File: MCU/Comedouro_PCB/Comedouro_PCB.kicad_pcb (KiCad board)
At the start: 2 copper layers, 19 parts, among them J1 Conn_02x10_Odd_Even, J2 Conn_02x10_Odd_Even, J5 HC-SR04, M1 Motor_Servo, Q1 Q_NPN_CBE, SW1 SW_Push, SW2 SW_Push, SW3 SW_Push, SW4 SW_Push, SW5 SW_Push

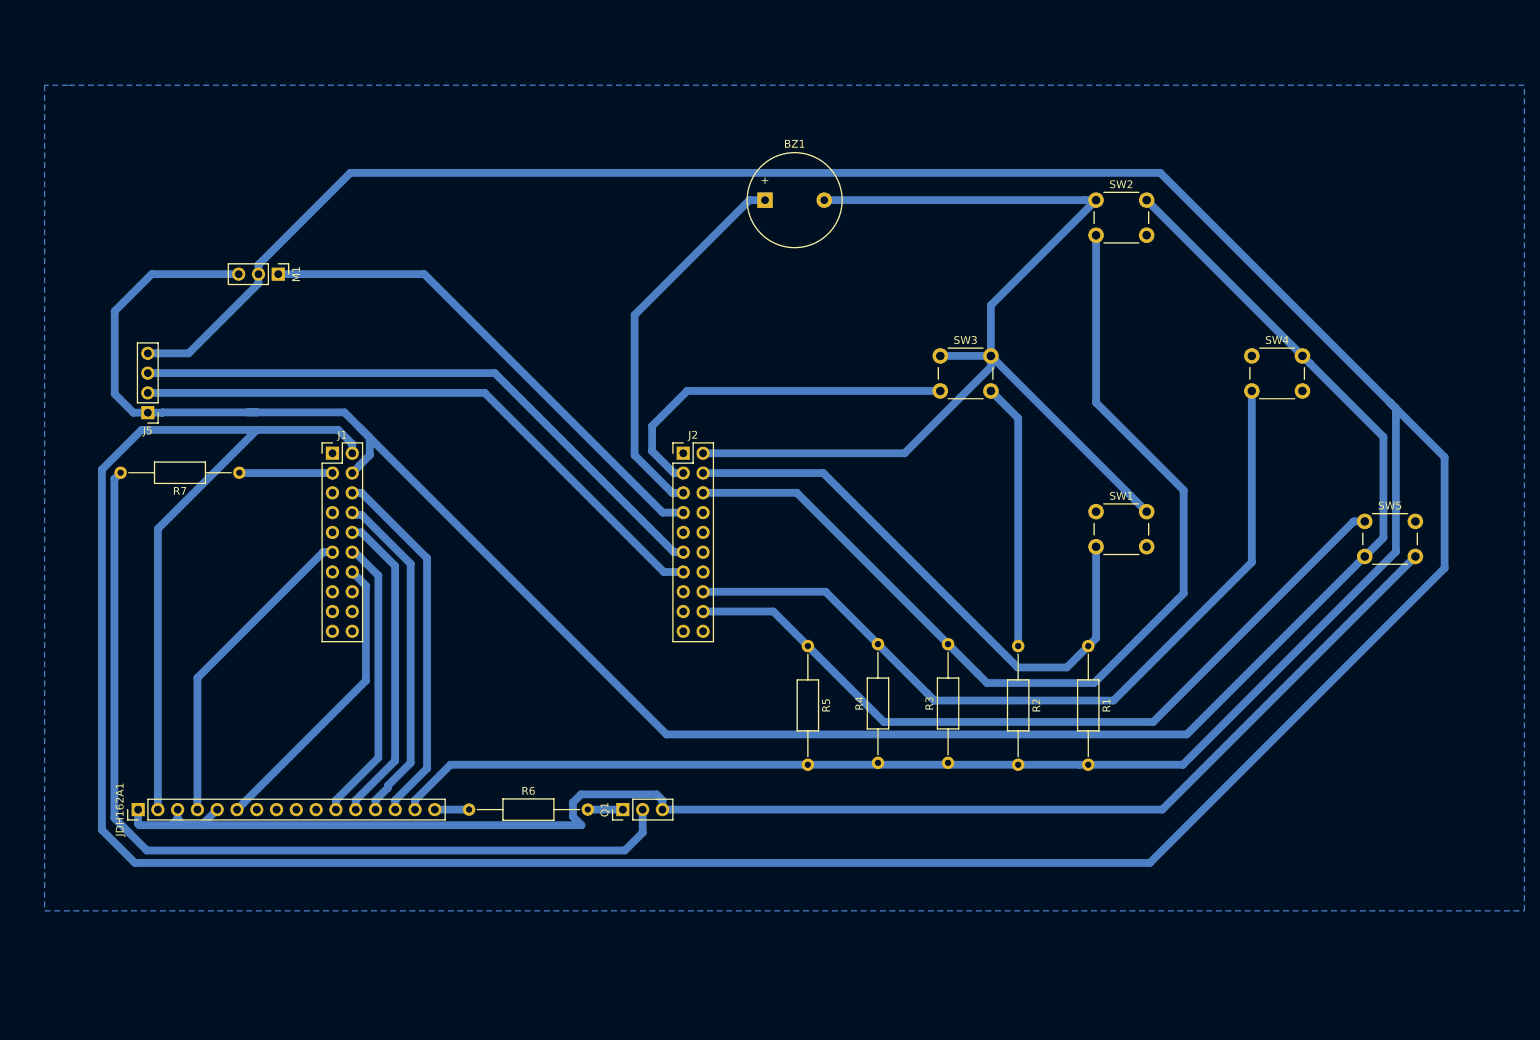
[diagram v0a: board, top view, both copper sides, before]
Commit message: PCB versão 3 e HD44780 com port
Signed-off-by: raulscr <raulsfreitas1997@hotmail.com>
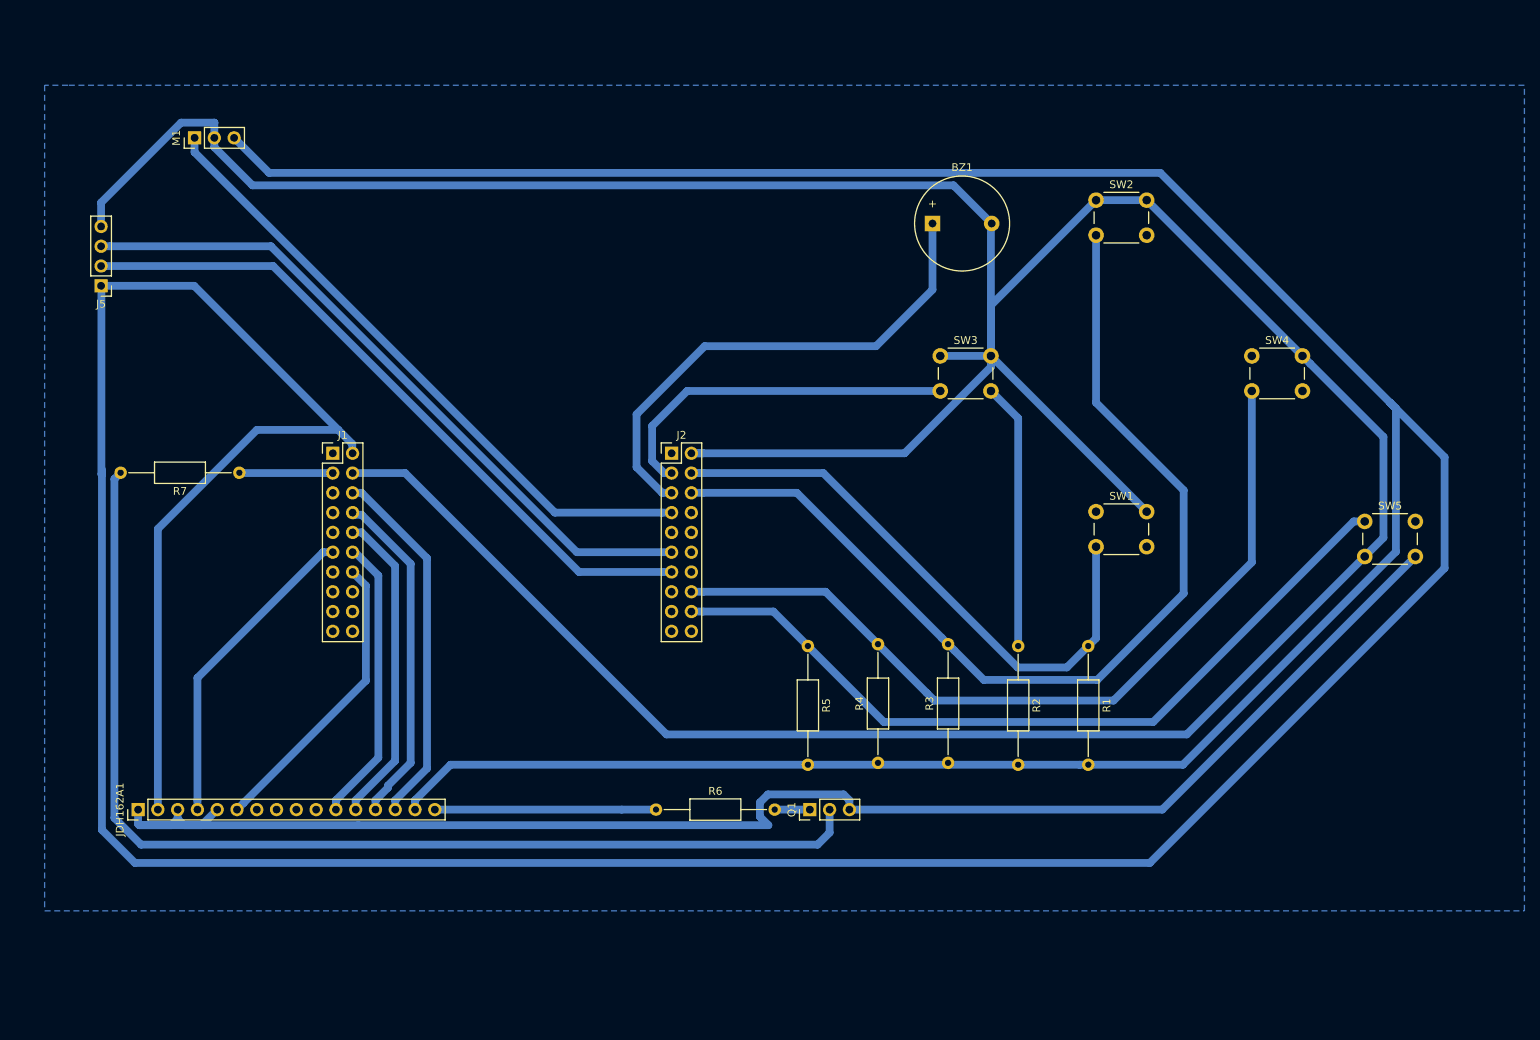
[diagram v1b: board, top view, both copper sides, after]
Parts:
- moved Q1 24.0 mm to (138.2, 137.0)
- moved R6 24.0 mm to (118.5, 137.0)
- moved BZ1 21.7 mm to (154.0, 61.8)
- moved M1 20.5 mm to (59.2, 50.8), turned to 90 degrees
- moved J5 17.4 mm to (47.2, 69.8)
- moved J2 1.50 mm to (120.5, 91.2)
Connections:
- J5 pad 1: GNDPWR -> +5V
- J5 pad 4: +5V -> GNDPWR
- M1 pad 2: +5V -> GNDPWR
- M1 pad 3: GNDPWR -> +5V
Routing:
- net GNDPWR: track 617.0 -> 669.4 mm
- net Net-(JDH162A1-Pad16): track 4.40 -> 28.4 mm
- net Net-(Q1-Pad2): track 118.1 -> 141.5 mm
- net +5V: track 693.0 -> 712.9 mm
- net Net-(J2-Pad7): track 64.7 -> 82.3 mm
- net Net-(BZ1-Pad1): track 49.1 -> 65.8 mm
- net Net-(J2-Pad13): track 78.3 -> 89.5 mm
- net Net-(J2-Pad11): track 78.3 -> 89.5 mm
- net Net-(J2-Pad4): track 74.1 -> 76.6 mm
- net Net-(J2-Pad18): track 101.5 -> 102.5 mm
- net Net-(J2-Pad16): track 105.6 -> 106.6 mm
- net Net-(J2-Pad3): track 81.5 -> 80.7 mm
- net Net-(J2-Pad6): track 127.3 -> 127.9 mm

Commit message: Ajeitando configuracoes
Signed-off-by: Wall Berg Morais <wallbergmirandamorais@gmail.com>
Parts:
- moved M1 154.5 mm to (193.3, 127.4), turned to 180 degrees
- moved J5 151.4 mm to (193.6, 108.6), turned to 0 degrees
- moved JDH162A1 99.8 mm to (117.1, 61.4)
- moved BZ1 92.6 mm to (114.8, 145.7)
- moved R2 68.2 mm to (97.3, 107.3), turned to 90 degrees
- moved R1 65.5 mm to (109.0, 107.6), turned to 0 degrees
- moved SW5 59.8 mm to (152.7, 118.5)
- moved SW3 55.4 mm to (152.9, 134.1)
- moved SW2 49.3 mm to (152.6, 102.7)
- moved R3 48.1 mm to (112.3, 110.9), turned to 270 degrees
- moved SW4 47.0 mm to (170.4, 118.8)
- moved SW1 44.7 mm to (134.9, 118.5)
- moved Q1 40.1 mm to (118.2, 102.3), turned to 270 degrees
- moved R6 39.2 mm to (123.7, 98.2), turned to 180 degrees
- moved R4 36.4 mm to (116.6, 110.9), turned to 270 degrees
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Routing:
- net GNDPWR: track 669.4 -> 10.7 mm
- net Net-(J1-Pad6): track 47.0 -> 230.0 mm
- net Net-(J1-Pad8): track 43.7 -> 214.3 mm
- net Net-(J1-Pad10): track 40.7 -> 199.3 mm
- net Net-(J1-Pad12): track 36.9 -> 183.6 mm
- net Net-(J1-Pad14): track 38.1 -> 156.3 mm
- net Net-(Q1-Pad2): track 141.5 -> 38.0 mm
- net Net-(Q1-Pad1): track 4.51 -> 80.2 mm
- net Net-(J1-Pad11): track 40.9 -> 115.1 mm
- net Net-(J2-Pad7): track 82.3 -> 154.2 mm
- net Net-(J2-Pad11): track 89.5 -> 153.1 mm
- net Net-(J2-Pad3): track 80.7 -> 130.7 mm
- net Net-(J2-Pad13): track 89.5 -> 138.9 mm
- net Net-(J2-Pad6): track 127.9 -> 86.4 mm
- net Net-(J2-Pad4): track 76.6 -> 46.5 mm
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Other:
- net class Default: via_dia 1 -> 2; via_drill 0.8 -> 1.5
